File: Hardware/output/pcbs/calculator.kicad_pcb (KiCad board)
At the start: 2 copper layers, 70.5 x 143 mm, 46 parts, among them J1 Sharp_LCD

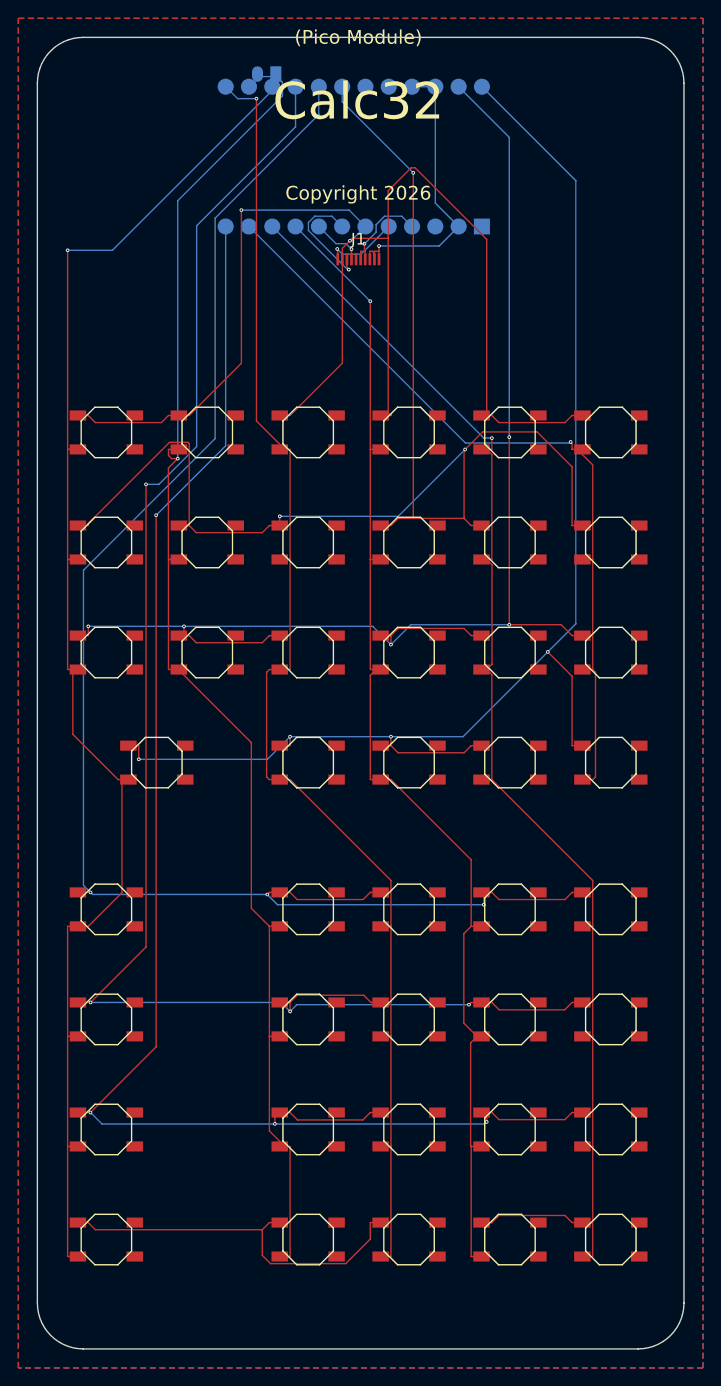
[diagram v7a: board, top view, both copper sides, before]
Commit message: refactor: rename C47 softkey infrastructure to generic softkey system and add hardware automation scripts
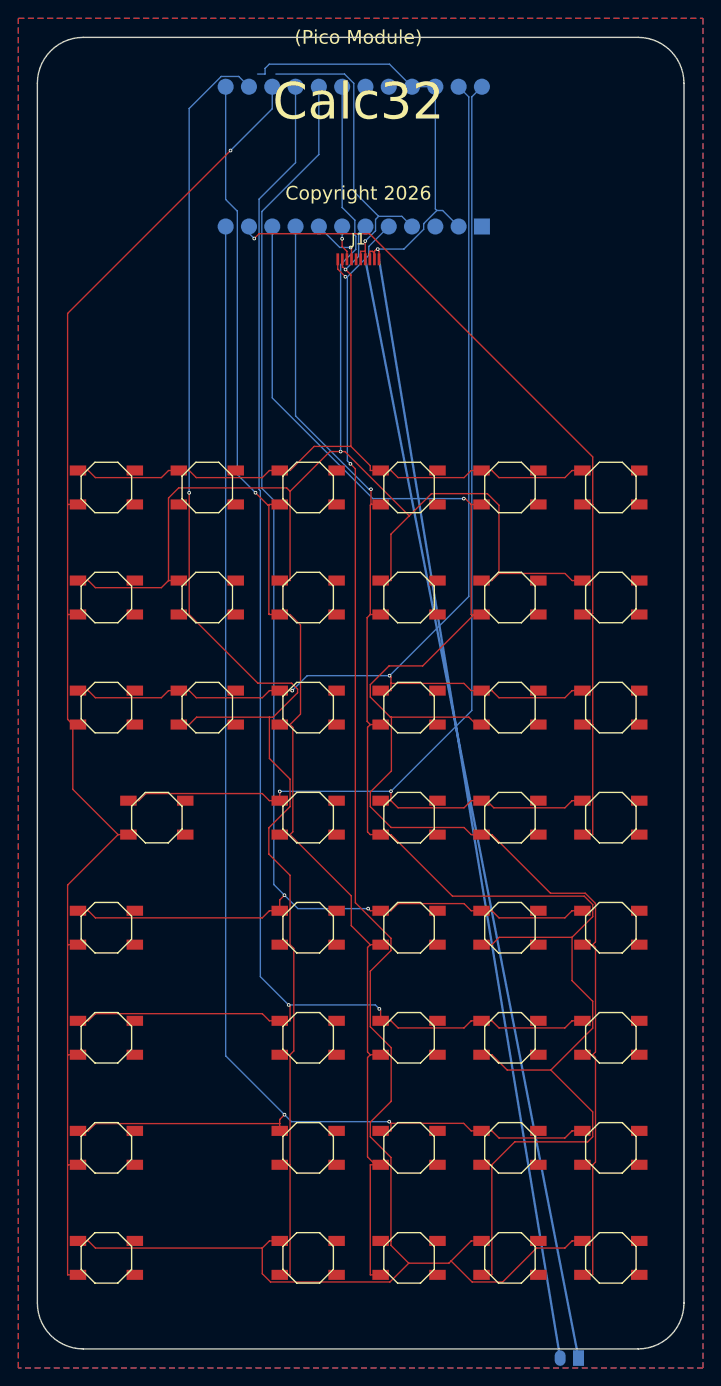
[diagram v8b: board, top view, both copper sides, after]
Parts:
- moved JST1 143.8 mm to (68.0, -8.00)
- moved B1 6.00 mm to (23.0, -66.9)
- moved B10 6.00 mm to (50.5, -78.9)
- moved B11 6.00 mm to (50.5, -90.9)
- moved B12 6.00 mm to (61.5, -66.9)
- moved B13 6.00 mm to (61.5, -78.9)
- moved B14 6.00 mm to (61.5, -90.9)
- moved B15 6.00 mm to (72.5, -66.9)
- moved B16 6.00 mm to (72.5, -78.9)
- moved B17 6.00 mm to (72.5, -90.9)
- moved B2 6.00 mm to (17.5, -78.9)
- moved B3 6.00 mm to (17.5, -90.9)
- moved B4 6.00 mm to (28.5, -78.9)
- moved B5 6.00 mm to (28.5, -90.9)
- moved B6 6.00 mm to (39.5, -66.9)
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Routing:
- net VCC: track 10.4 -> 157.3 mm
- net GND: track 32.7 -> 171.8 mm
- net P21: track 61.5 -> 193.7 mm, vias 1 -> 2
- net P20: track 152.9 -> 86.5 mm, vias 2 -> 1
- net P15: track 130.3 -> 177.1 mm
- net P14: track 136.7 -> 173.9 mm
- net P5: track 169.7 -> 150.8 mm, vias 3 -> 2
- net P6: track 179.0 -> 163.4 mm, vias 4 -> 2
- net P0: track 144.4 -> 128.9 mm, vias 5 -> 2
- net P10: track 173.7 -> 159.6 mm, vias 4 -> 2
- net P8: track 152.0 -> 164.3 mm
- net P1: track 146.4 -> 135.5 mm, vias 4 -> 2
- net P19: track 12.7 -> 3.80 mm
- net P4: track 151.9 -> 143.5 mm, vias 3 -> 1
- net P16: track 87.2 -> 94.4 mm
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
